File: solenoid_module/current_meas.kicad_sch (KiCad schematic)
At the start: 2 parts, among them U1 TMCS1107A3

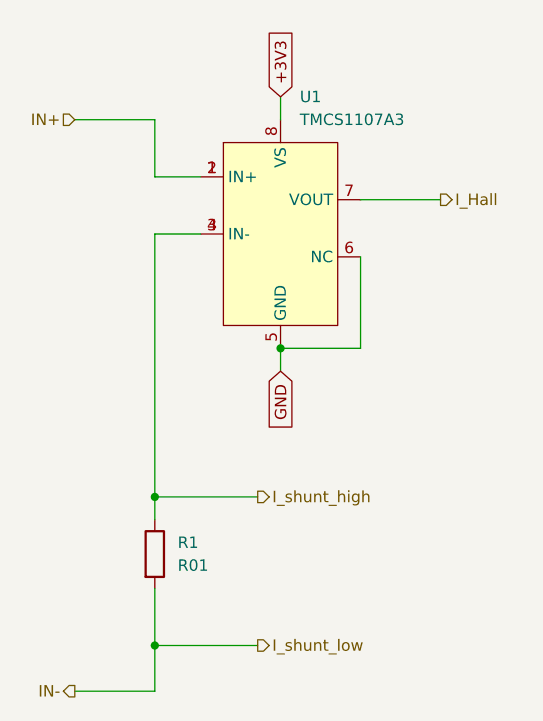
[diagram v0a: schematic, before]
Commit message: Solenoid module wiring
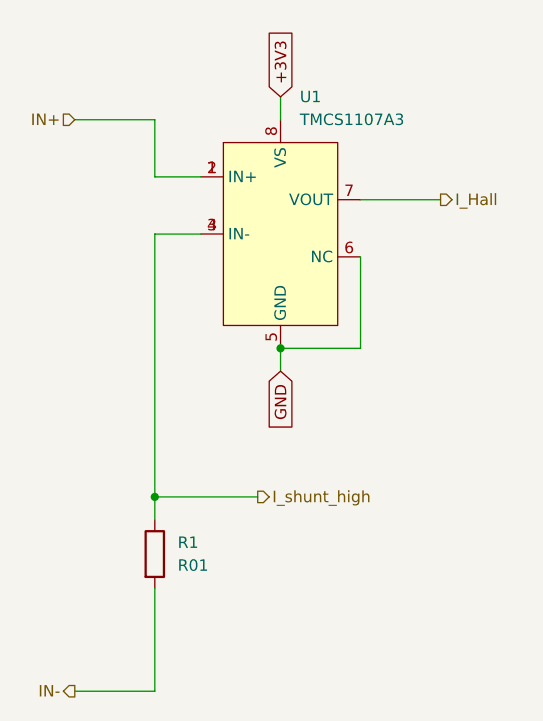
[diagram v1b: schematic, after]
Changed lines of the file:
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@@
-		(color 0 0 0 0)
-	)
-	(junction
-		(at 40.64 87.63)
-		(diameter 0)
 		(color 0 0 0 0)
 	)
@@
 		(pts
 			(xy 40.64 73.66) (xy 40.64 71.12)
-		)
-		(stroke
-			(width 0)
-			(type default)
-		)
-	)
-	(wire
-		(pts
-			(xy 40.64 87.63) (xy 52.07 87.63)
 		)
 		(stroke
@@
 	(wire
 		(pts
-			(xy 40.64 81.28) (xy 40.64 87.63)
+			(xy 40.64 81.28) (xy 40.64 92.71)
 		)
 		(stroke
@@
 		(pts
 			(xy 40.64 71.12) (xy 52.07 71.12)
-		)
-		(stroke
-			(width 0)
-			(type default)
-		)
-	)
-	(wire
-		(pts
-			(xy 40.64 87.63) (xy 40.64 92.71)
 		)
 		(stroke
@@
 		)
 	)
-	(hierarchical_label "I_shunt_low"
-		(shape output)
-		(at 52.07 87.63 0)
-		(effects
-			(font
-				(size 1.27 1.27)
-			)
-			(justify left)
-		)
-	)
